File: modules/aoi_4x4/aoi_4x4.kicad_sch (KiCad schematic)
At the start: 44 parts, among them J1 Conn_02x12_Odd_Even, Q1 2N3906, Q10 2N3906, Q11 2N3906, Q12 2N3906, Q13 2N3906, Q14 2N3906, Q15 2N3906, Q16 2N3906, Q17 2N3906, Q18 2N3906, Q19 2N3906, Q2 2N3904, Q20 2N3906, Q21 2N3906, Q22 2N3904, Q23 2N3904, Q3 2N3904, Q4 2N3904, Q5 2N3906, Q6 2N3906, Q7 2N3906, Q8 2N3904, Q9 2N3904

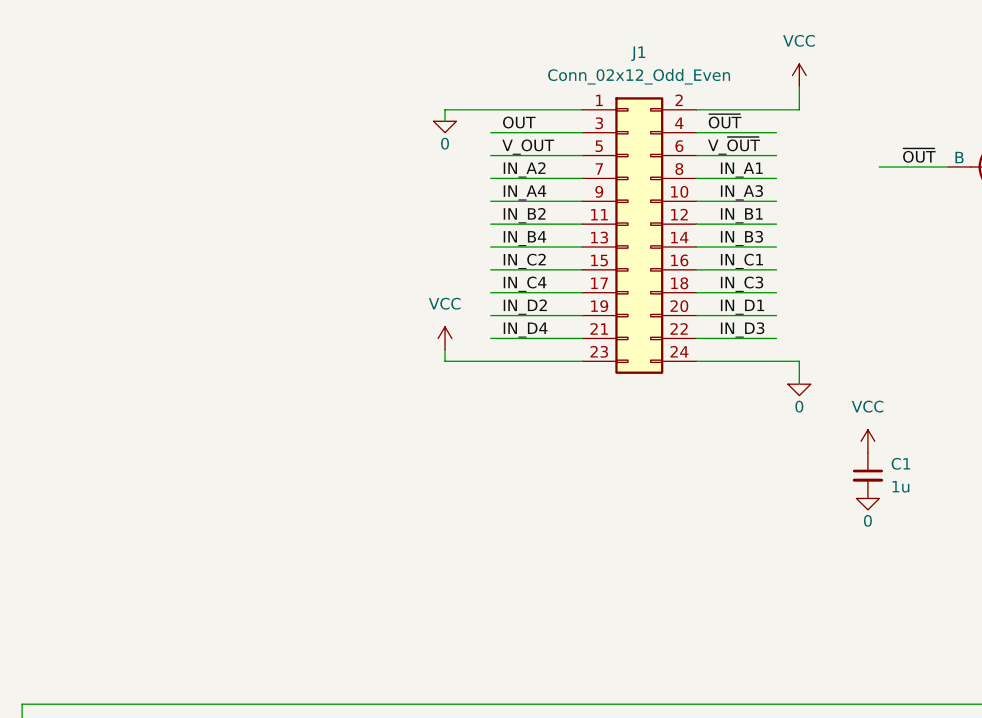
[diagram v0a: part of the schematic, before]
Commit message: Started working towards real modules. Modules with PCIe connectors.
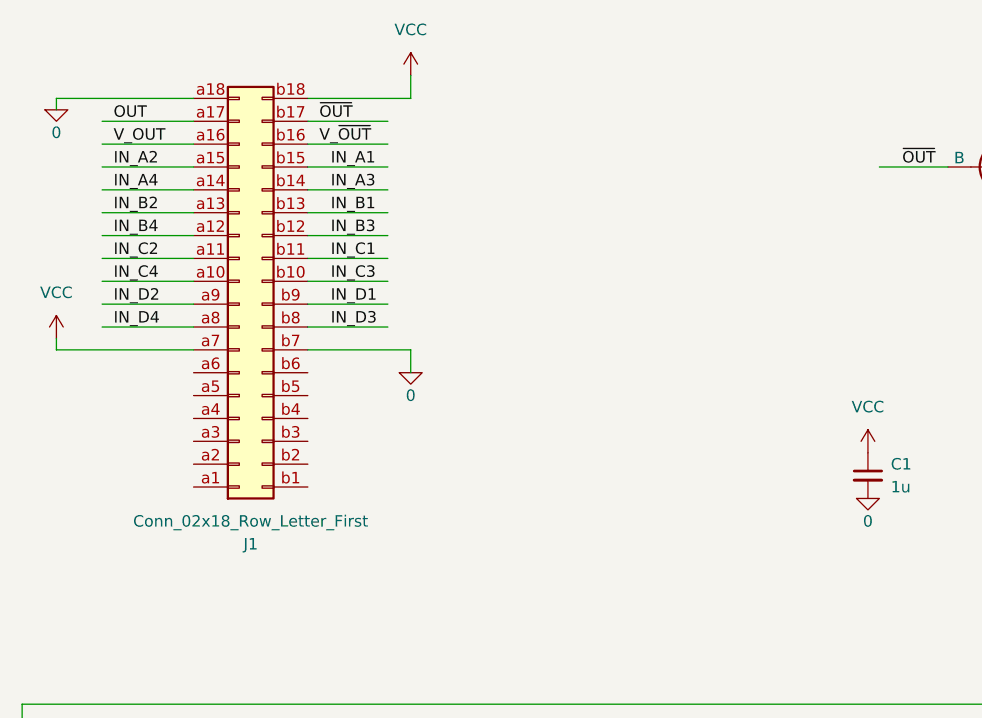
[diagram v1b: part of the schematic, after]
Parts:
- removed J1: Conn_02x12_Odd_Even, Connector_PinHeader_2.54mm:PinHeader_2x12_P2.54mm_Horizontal, symbol Connector_Generic:Conn_02x12_Odd_Even
- added J1: Conn_02x18_Row_Letter_First, Connector_PCBEdge:BUS_PCIexpress_x1, symbol Connector_Generic:Conn_02x18_Row_Letter_First
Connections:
- net 0: now also J1.a18 (Pin_a18), J1.b7 (Pin_b7)
- net IN_A1: now also J1.b15 (Pin_b15)
- net IN_A2: now also J1.a15 (Pin_a15)
- net IN_A3: now also J1.b14 (Pin_b14)
- net IN_A4: now also J1.a14 (Pin_a14)
- net IN_B1: now also J1.b13 (Pin_b13)
- net IN_B2: now also J1.a13 (Pin_a13)
- net IN_B3: now also J1.b12 (Pin_b12)
- net IN_B4: now also J1.a12 (Pin_a12)
- net IN_C1: now also J1.b11 (Pin_b11)
- net IN_C2: now also J1.a11 (Pin_a11)
- net IN_C3: now also J1.b10 (Pin_b10)
- net IN_C4: now also J1.a10 (Pin_a10)
- net IN_D1: now also J1.b9 (Pin_b9)
- net IN_D2: now also J1.a9 (Pin_a9)
- net IN_D3: now also J1.b8 (Pin_b8)
- net IN_D4: now also J1.a8 (Pin_a8)
- net OUT: now also J1.a17 (Pin_a17)
- net VCC: now also J1.a7 (Pin_a7), J1.b18 (Pin_b18)
- net V_OUT: now also J1.a16 (Pin_a16)
- net V_~{OUT}: now also J1.b16 (Pin_b16)
- net ~{OUT}: now also J1.b17 (Pin_b17)

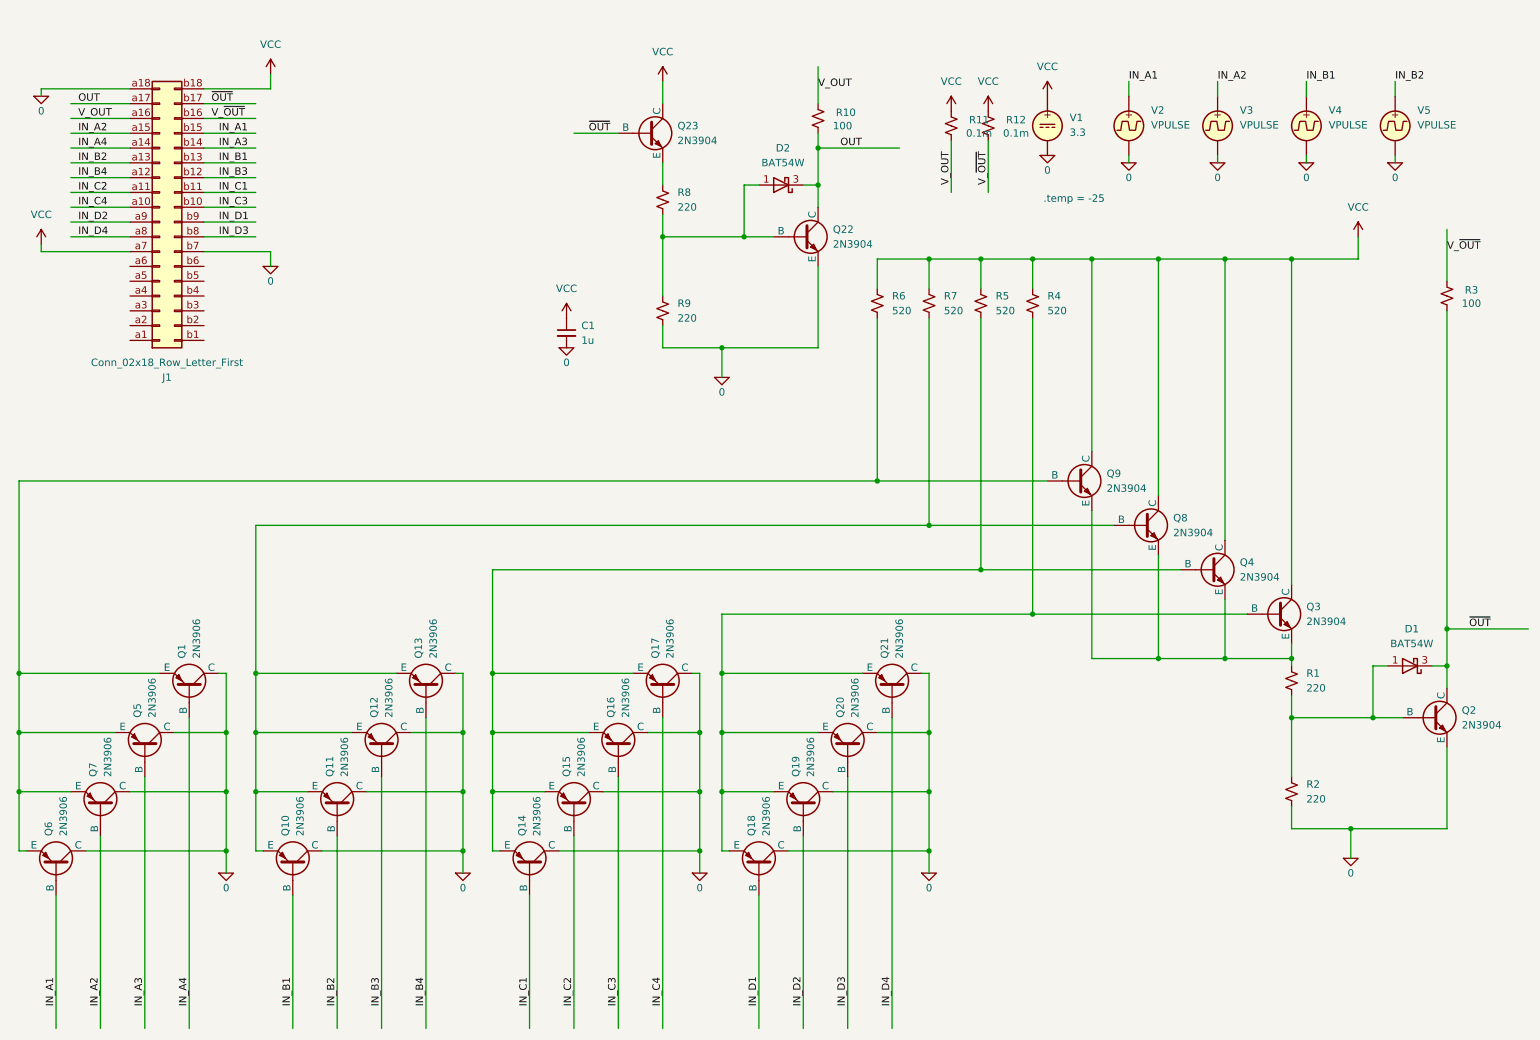
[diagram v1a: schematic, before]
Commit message: Started PCIe connector-based module design.
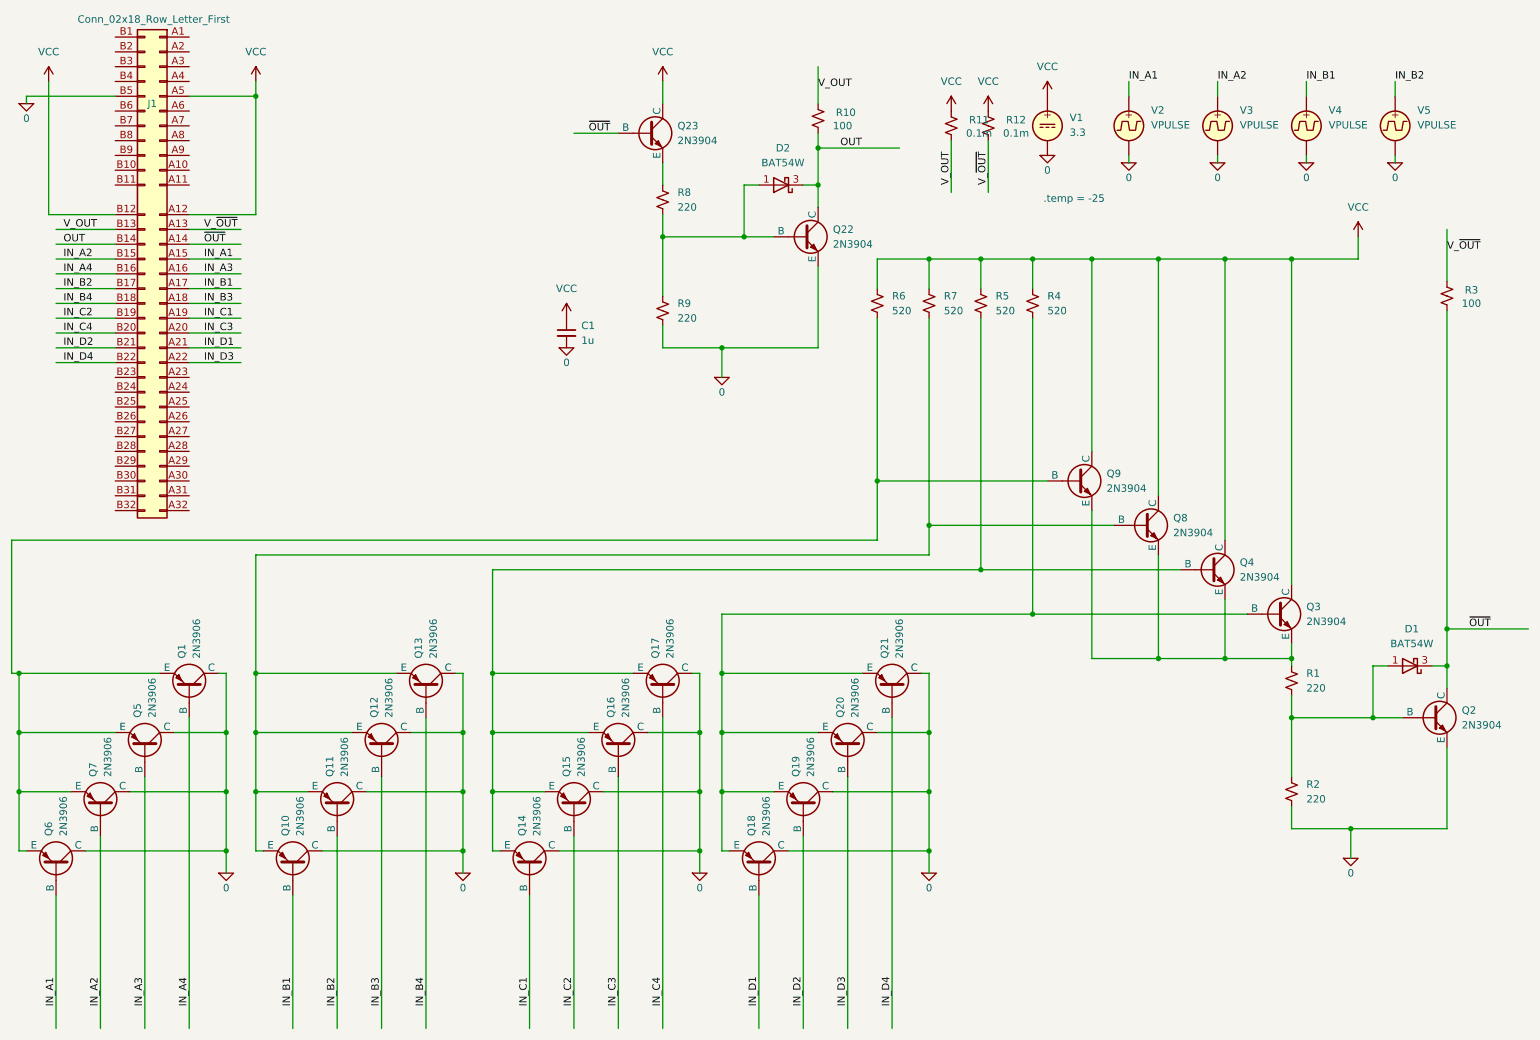
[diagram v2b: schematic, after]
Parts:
- J1: footprint Connector_PCBEdge:BUS_PCIexpress_x1 -> Connector_PCBEdge:BUS_PCIexpress_x4; symbol Connector_Generic:Conn_02x18_Row_Letter_First -> tcomp:PCIe_4x_edge; now in the parts list
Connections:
- net 0: now also J1.B5 (Pin_b5); no longer J1.a18 (Pin_a18), J1.b7 (Pin_b7)
- net IN_A1: now also J1.A15 (Pin_a15); no longer J1.b15 (Pin_b15)
- net IN_A2: now also J1.B15 (Pin_b15); no longer J1.a15 (Pin_a15)
- net IN_A3: now also J1.A16 (Pin_a16); no longer J1.b14 (Pin_b14)
- net IN_A4: now also J1.B16 (Pin_b16); no longer J1.a14 (Pin_a14)
- net IN_B1: now also J1.A17 (Pin_a17); no longer J1.b13 (Pin_b13)
- net IN_B2: now also J1.B17 (Pin_b17); no longer J1.a13 (Pin_a13)
- net IN_B3: now also J1.A18 (Pin_a18); no longer J1.b12 (Pin_b12)
- net IN_B4: now also J1.B18 (Pin_b18); no longer J1.a12 (Pin_a12)
- net IN_C1: now also J1.A19 (Pin_a19); no longer J1.b11 (Pin_b11)
- net IN_C2: now also J1.B19 (Pin_b19); no longer J1.a11 (Pin_a11)
- net IN_C3: now also J1.A20 (Pin_a20); no longer J1.b10 (Pin_b10)
- net IN_C4: now also J1.B20 (Pin_b20); no longer J1.a10 (Pin_a10)
- net IN_D1: now also J1.A21 (Pin_a21); no longer J1.b9 (Pin_b9)
- net IN_D2: now also J1.B21 (Pin_b21); no longer J1.a9 (Pin_a9)
- net IN_D3: now also J1.A22 (Pin_a22); no longer J1.b8 (Pin_b8)
- net IN_D4: now also J1.B22 (Pin_b22); no longer J1.a8 (Pin_a8)
- net OUT: now also J1.B14 (Pin_b14); no longer J1.a17 (Pin_a17)
- net VCC: now also J1.A12 (Pin_a12), J1.A5 (Pin_a5), J1.B12 (Pin_b12); no longer J1.a7 (Pin_a7), J1.b18 (Pin_b18)
- net V_OUT: now also J1.B13 (Pin_b13); no longer J1.a16 (Pin_a16)
- net V_~{OUT}: now also J1.A13 (Pin_a13); no longer J1.b16 (Pin_b16)
- net ~{OUT}: now also J1.A14 (Pin_a14); no longer J1.b17 (Pin_b17)

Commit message: More work on AOI PCB. Fully routed, but not clean yet.
Also needs bypass caps.
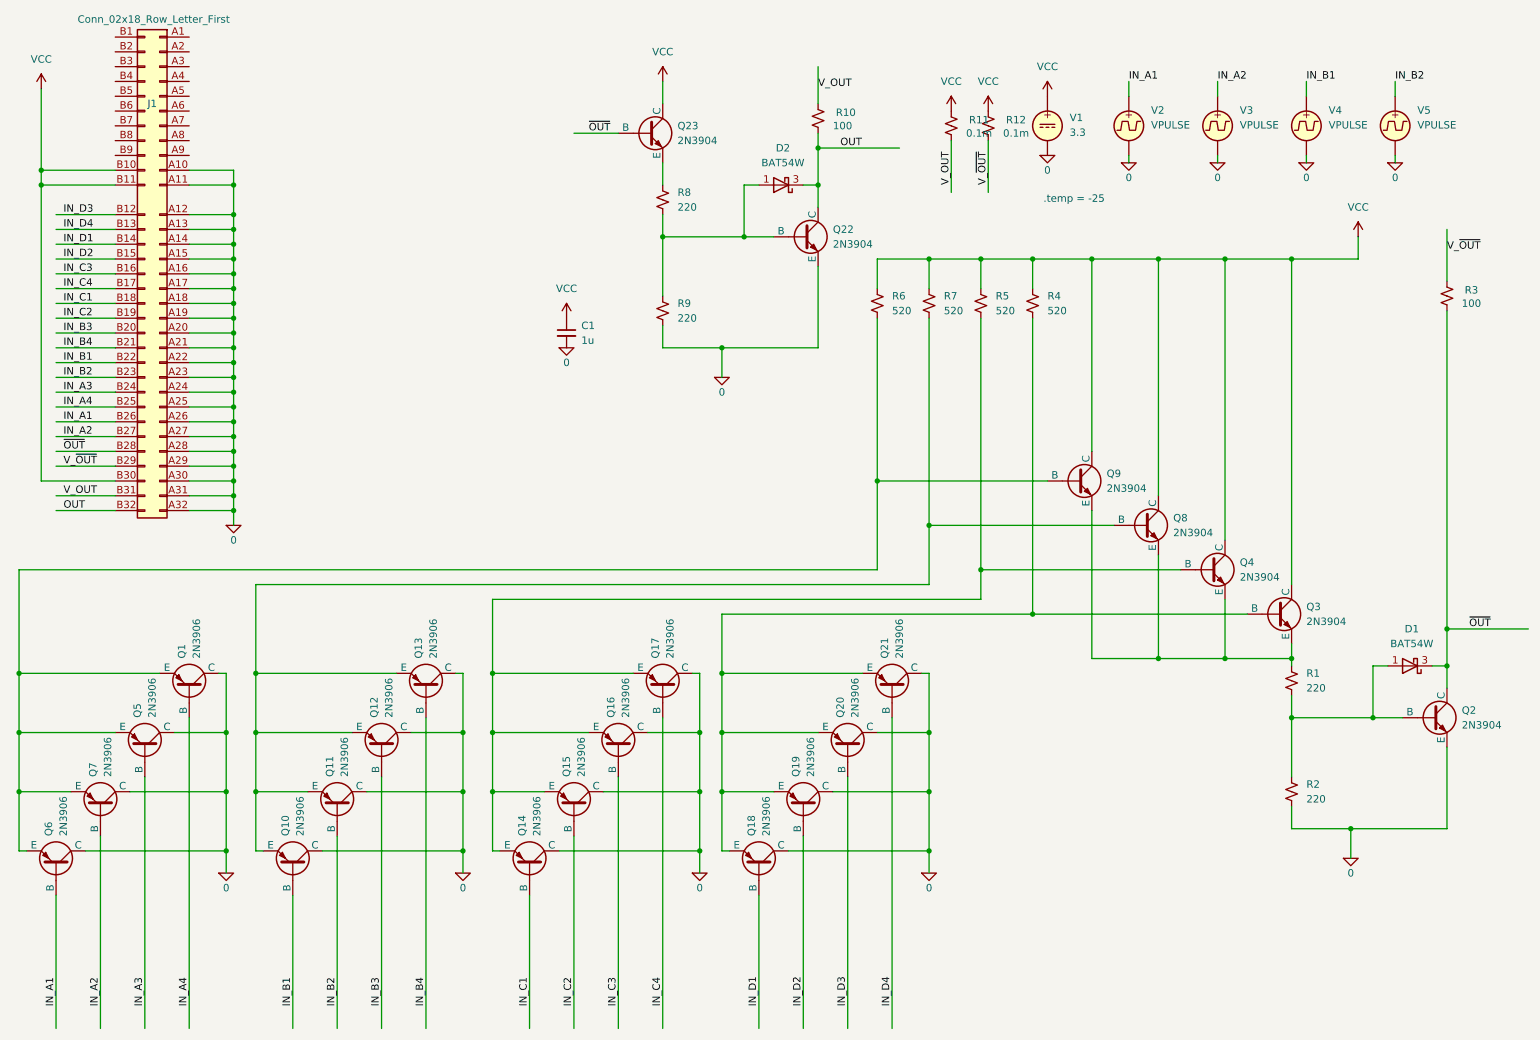
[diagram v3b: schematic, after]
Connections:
- net 0: now also J1.A10 (Pin_a10), J1.A11 (Pin_a11), J1.A12 (Pin_a12), J1.A13 (Pin_a13), J1.A14 (Pin_a14), J1.A15 (Pin_a15), J1.A16 (Pin_a16), J1.A17 (Pin_a17), J1.A18 (Pin_a18), J1.A19 (Pin_a19), J1.A20 (Pin_a20), J1.A21 (Pin_a21), J1.A22 (Pin_a22), J1.A23 (Pin_a23), J1.A24 (Pin_a24), J1.A25 (Pin_a25), J1.A26 (Pin_a26), J1.A27 (Pin_a27), J1.A28 (Pin_a28), J1.A29 (Pin_a29), J1.A30 (Pin_a30), J1.A31 (Pin_a31), J1.A32 (Pin_a32); no longer J1.B5 (Pin_b5)
- net IN_A1: now also J1.B26 (Pin_b26); no longer J1.A15 (Pin_a15)
- net IN_A2: now also J1.B27 (Pin_b27); no longer J1.B15 (Pin_b15)
- net IN_A3: now also J1.B24 (Pin_b24); no longer J1.A16 (Pin_a16)
- net IN_A4: now also J1.B25 (Pin_b25); no longer J1.B16 (Pin_b16)
- net IN_B1: now also J1.B22 (Pin_b22); no longer J1.A17 (Pin_a17)
- net IN_B2: now also J1.B23 (Pin_b23); no longer J1.B17 (Pin_b17)
- net IN_B3: now also J1.B20 (Pin_b20); no longer J1.A18 (Pin_a18)
- net IN_B4: now also J1.B21 (Pin_b21); no longer J1.B18 (Pin_b18)
- net IN_C1: now also J1.B18 (Pin_b18); no longer J1.A19 (Pin_a19)
- net IN_C3: now also J1.B16 (Pin_b16); no longer J1.A20 (Pin_a20)
- net IN_C4: now also J1.B17 (Pin_b17); no longer J1.B20 (Pin_b20)
- net IN_D1: now also J1.B14 (Pin_b14); no longer J1.A21 (Pin_a21)
- net IN_D2: now also J1.B15 (Pin_b15); no longer J1.B21 (Pin_b21)
- net IN_D3: now also J1.B12 (Pin_b12); no longer J1.A22 (Pin_a22)
- net IN_D4: now also J1.B13 (Pin_b13); no longer J1.B22 (Pin_b22)
- net OUT: now also J1.B32 (Pin_b32); no longer J1.B14 (Pin_b14)
- net VCC: now also J1.B10 (Pin_b10), J1.B11 (Pin_b11), J1.B30 (Pin_b30); no longer J1.A12 (Pin_a12), J1.A5 (Pin_a5), J1.B12 (Pin_b12)
- net V_OUT: now also J1.B31 (Pin_b31); no longer J1.B13 (Pin_b13)
- net V_~{OUT}: now also J1.B29 (Pin_b29); no longer J1.A13 (Pin_a13)
- net ~{OUT}: now also J1.B28 (Pin_b28); no longer J1.A14 (Pin_a14)

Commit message: More flushed out library and it's use. PCB is also much nicer.
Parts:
- removed D1, D2: BAT54W, Package_TO_SOT_SMD:SOT-323_SC-70, symbol Diode:BAT54W
- added D1, D2: BAT54LT1G, Package_TO_SOT_SMD:SOT-23-3, symbol tcomp:BAT54LT1G
- added V6, V7, V8, V9: VPULSE, symbol Simulation_SPICE:VPULSE
- J1: footprint Connector_PCBEdge:BUS_PCIexpress_x4 -> tcomp:BUS_PCIexpress_x4
- Q1, Q10, Q11, Q12, Q13, Q14, Q15, Q16, Q17, Q18, Q19, Q20, Q21, Q5, Q6, Q7: symbol Simulation_SPICE:PNP -> tcomp:2N3906
- Q2, Q22, Q23, Q3, Q4, Q8, Q9: symbol Simulation_SPICE:NPN -> tcomp:2N3904
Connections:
- net IN_C1: now also V6.1
- net IN_C2: now also V7.1
- net IN_D1: now also V8.1
- net IN_D2: now also V9.1
- net OUT: now also D2.3 (K)
- net ~{OUT}: now also D1.3 (K)
- net A: now reaches Q1.3 (E), Q5.3 (E), Q6.3 (E), Q7.3 (E), Q9.2 (B), R6.2
- net X: now reaches Q3.3 (E), Q4.3 (E), Q8.3 (E), Q9.3 (E), R1.1
- net B: now reaches Q10.3 (E), Q11.3 (E), Q12.3 (E), Q13.3 (E), Q8.2 (B), R7.2
- net Y2: now reaches Q22.2 (B), R8.2, R9.1
- net Y2: now also D2.1 (A)
- net C: now reaches Q14.3 (E), Q15.3 (E), Q16.3 (E), Q17.3 (E), Q4.2 (B), R5.2
- net X2: now reaches Q2.2 (B), R1.2, R2.1
- net X2: now also D1.1 (A)
- net D: now reaches Q18.3 (E), Q19.3 (E), Q20.3 (E), Q21.3 (E), Q3.2 (B), R4.2
- net Y: now reaches Q23.3 (E), R8.1
- net 0 renamed GND
- net GND: now also V6.2, V7.2, V8.2, V9.2
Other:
- moved on the sheet: C1, Q22, Q23, R10, R11, R12, R8, R9, V1, V2, V3, V4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
